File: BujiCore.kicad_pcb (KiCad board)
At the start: 6 copper layers, 27 x 50.5 mm, 209 parts, among them J1 Micro_SD_Card_Det, J2 SYS_UART, Q1 BSN20, SW1 SW_Push, U1 ALLWINNER-H5(FBGA-347), U10 K4B8G1646Q-MYK0(FBGA-96_512MX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, U11 PT5110E23C-33, U12 KLMAG1JETD-B041, U2 RT8059GJ5, U3 K4B8G1646Q-MYK0(FBGA-96_512MX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

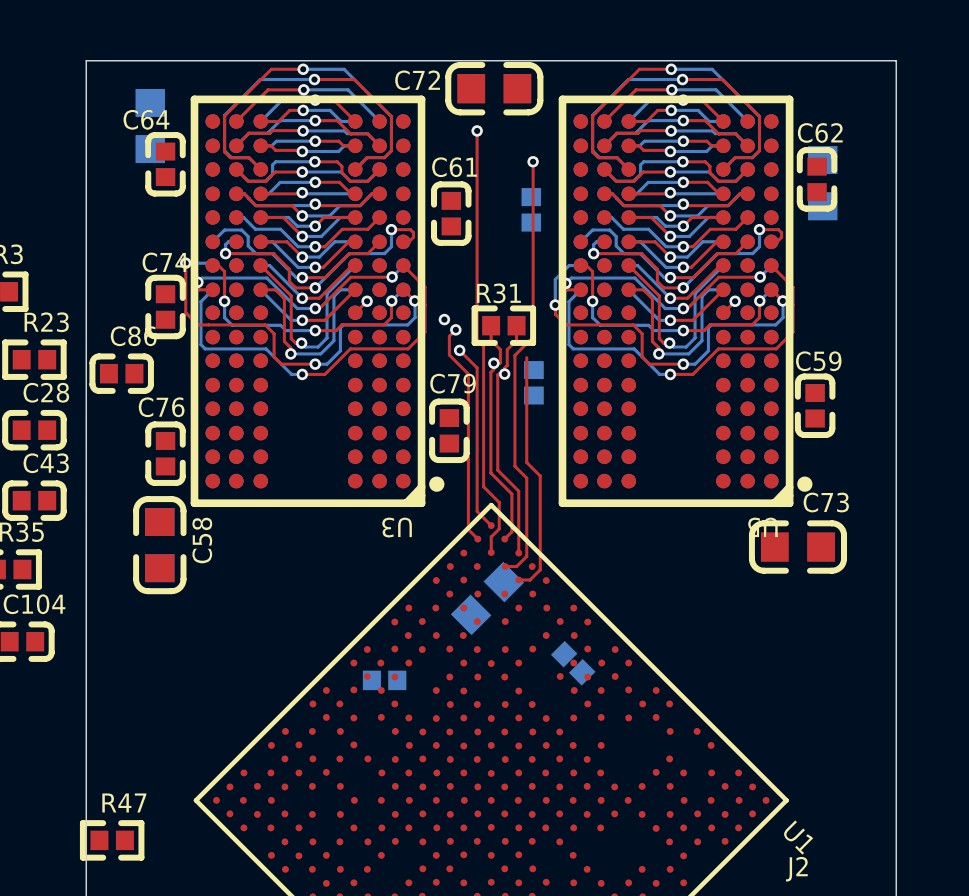
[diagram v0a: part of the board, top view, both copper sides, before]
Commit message: 完成了许多T点到芯片的拉线工作
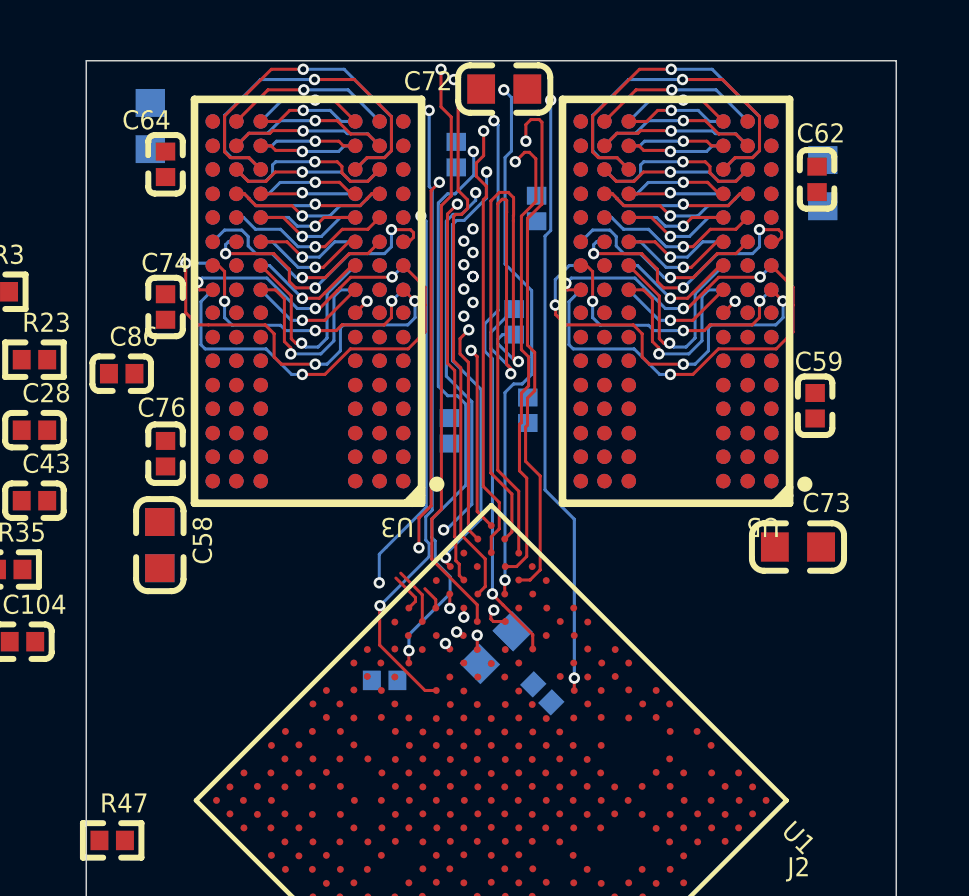
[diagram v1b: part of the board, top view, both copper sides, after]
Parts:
- C61, C79, R31: moved to B.Cu
- moved C61 1.98 mm to (-1.17, -51.4)
- moved C53 1.66 mm to (0.17, -34.9)
- moved C75 1.44 mm to (1.70, -33.4)
- moved C80 0.94 mm to (1.22, -42.8)
- moved R31 0.37 mm to (0.76, -45.8), turned to -90 degrees
- moved C72 0.33 mm to (0.43, -53.6)
- moved C77 0.18 mm to (1.51, -49.6)
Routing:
- net /CPU_RAM/SA14: track 19.2 -> 40.4 mm, vias 2 -> 4
- net /CPU_RAM/SBA1: track 23.0 -> 43.4 mm, vias 2 -> 5
- net /CPU_RAM/SA13: track 19.7 -> 39.9 mm, vias 2 -> 4
- net /CPU_RAM/SA11: track 18.9 -> 38.5 mm, vias 2 -> 4
- net /CPU_RAM/SA1: track 36.5 -> 55.9 mm, vias 2 -> 3
- net /CPU_RAM/SA0: track 19.2 -> 38.5 mm, vias 2 -> 5
- net /CPU_RAM/SA7: track 23.2 -> 41.7 mm, vias 2 -> 4
- net /CPU_RAM/SA2: track 35.9 -> 54.1 mm, vias 2 -> 3
- net /CPU_RAM/SA8: track 23.6 -> 41.5 mm, vias 2 -> 4
- net /CPU_RAM/SA12: track 18.6 -> 36.5 mm, vias 2 -> 5
- net /CPU_RAM/SBA2: track 19.4 -> 35.4 mm, vias 2 -> 4
- net /CPU_RAM/SA4: track 23.0 -> 37.7 mm, vias 2 -> 4
- net /CPU_RAM/SA3: track 22.6 -> 35.5 mm, vias 2 -> 3
- net /CPU_RAM/SCK_P: track 34.6 -> 47.3 mm
- net /CPU_RAM/SCK_N: track 34.9 -> 46.9 mm
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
